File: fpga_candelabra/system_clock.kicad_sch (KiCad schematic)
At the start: 21 parts, among them U22 CDCM6208V1, Y2 NX3225GA 25MHz

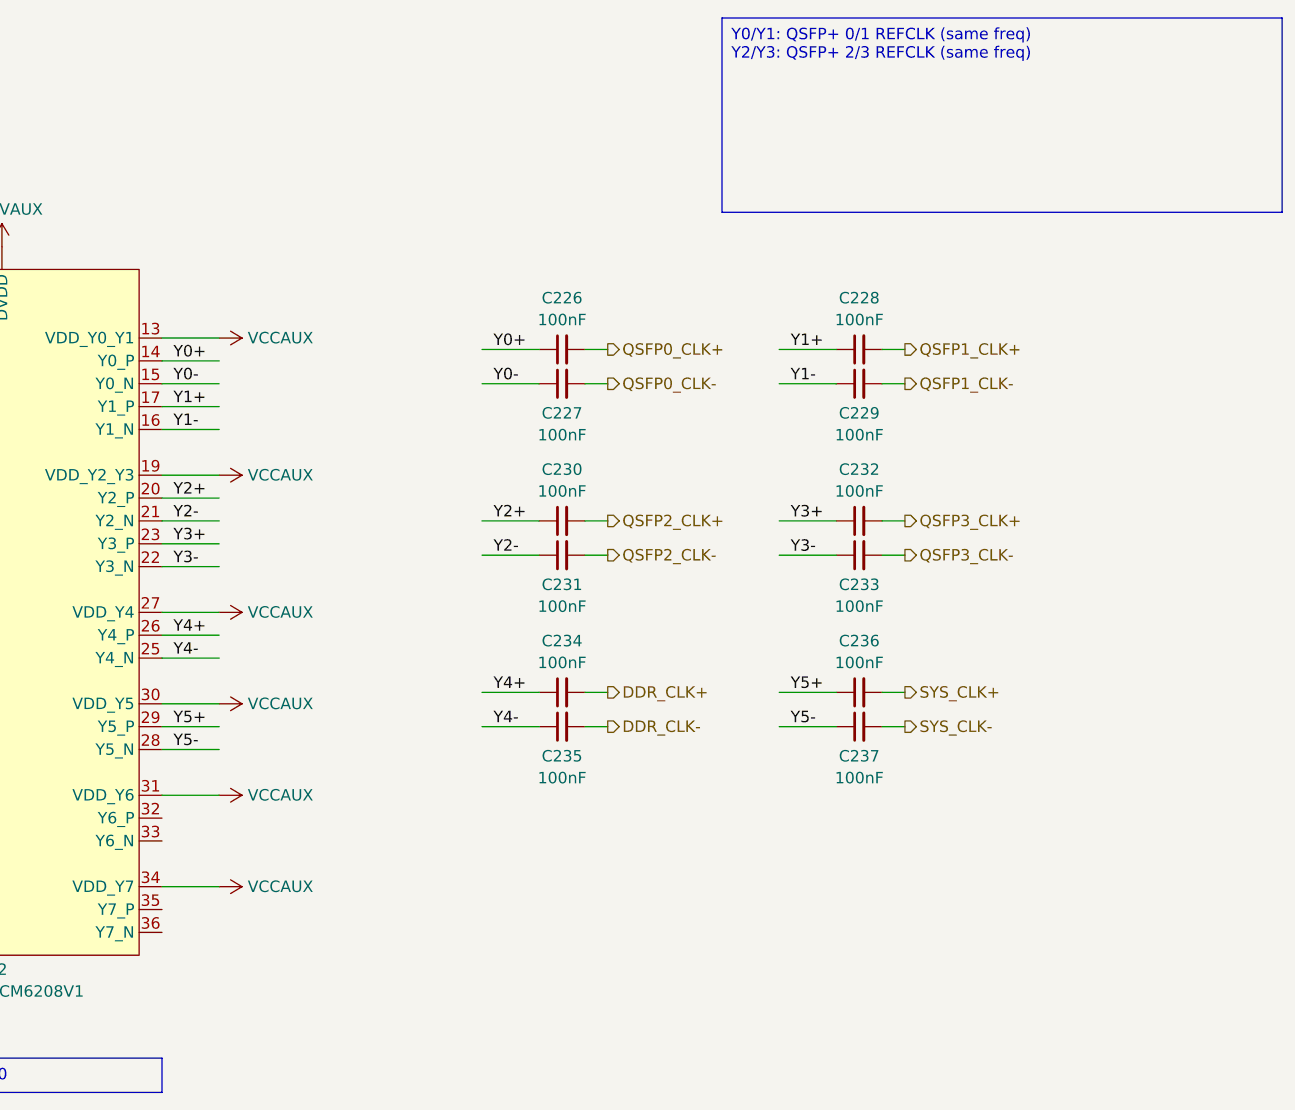
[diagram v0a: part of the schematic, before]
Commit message: candelabra: add i-pex extension ports, remove FMC1
* update bank/mgt allocation
* add basic pcb floorplanning

Signed-off-by: Yichuan Gao <gaoyichuan000@gmail.com>
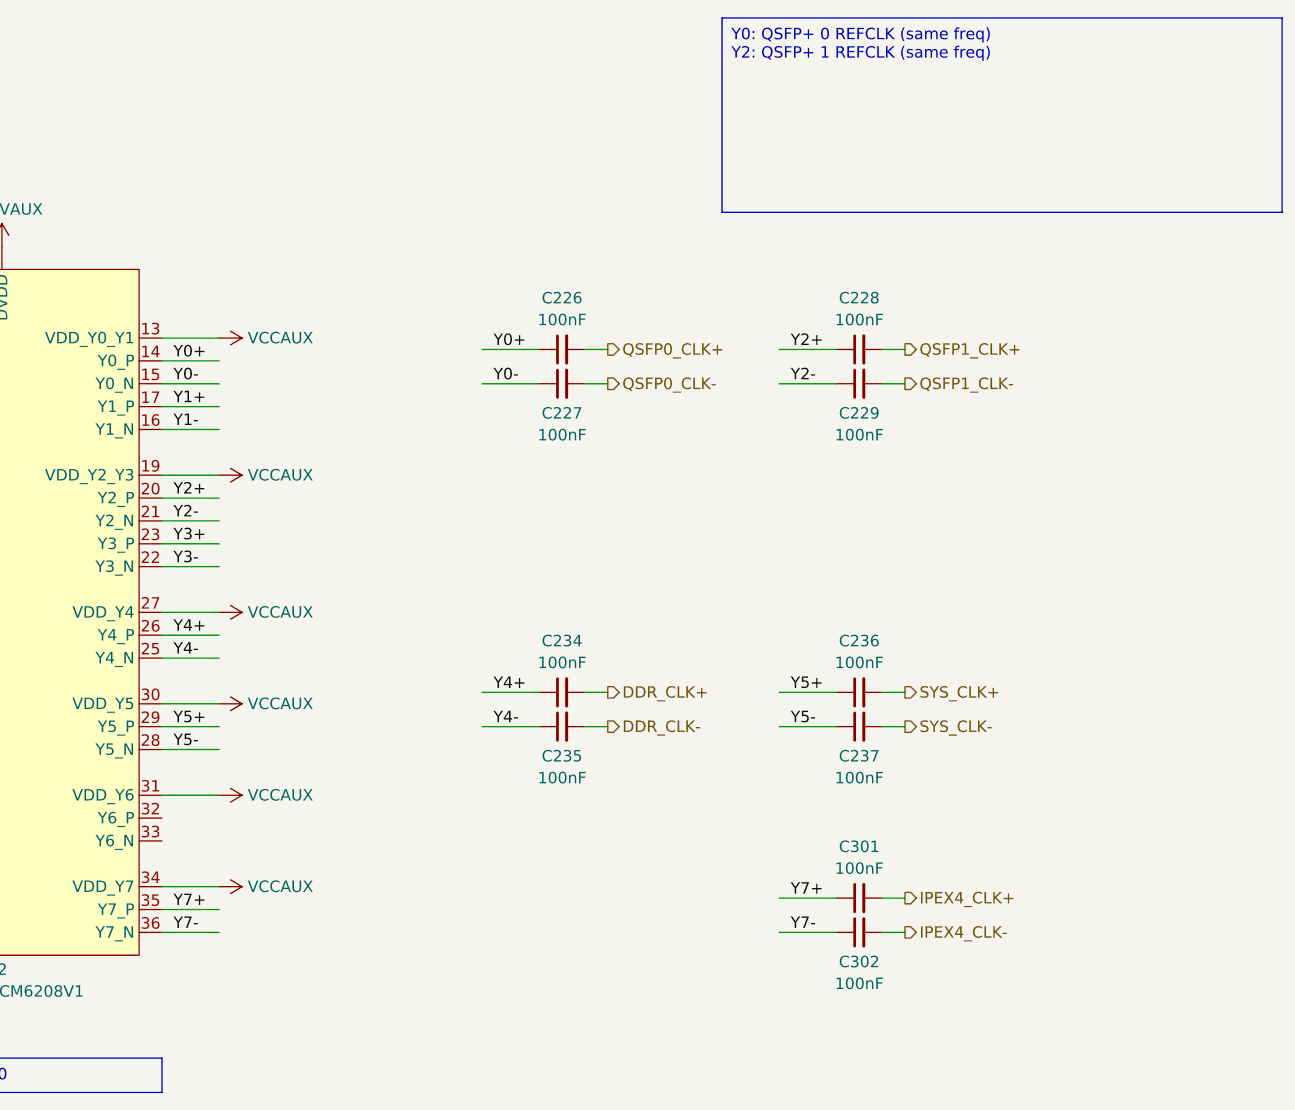
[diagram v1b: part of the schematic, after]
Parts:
- removed C230, C231, C232, C233: 100nF, Capacitor_SMD:C_0402_1005Metric, symbol Device:C_Small
- added C301, C302: 100nF, Capacitor_SMD:C_0402_1005Metric, symbol Device:C_Small
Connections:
- net Y1+: no longer C228.1
- net Y1-: no longer C229.1
- net Y2+: now also C228.1
- net Y2-: now also C229.1
- net Y7+: now reaches U22.35 (Y7_P)
- net Y7+: now also C301.1
- net Y7-: now reaches U22.36 (Y7_N)
- net Y7-: now also C302.1
- new net IPEX4_CLK+: C301.2
- new net IPEX4_CLK-: C302.2

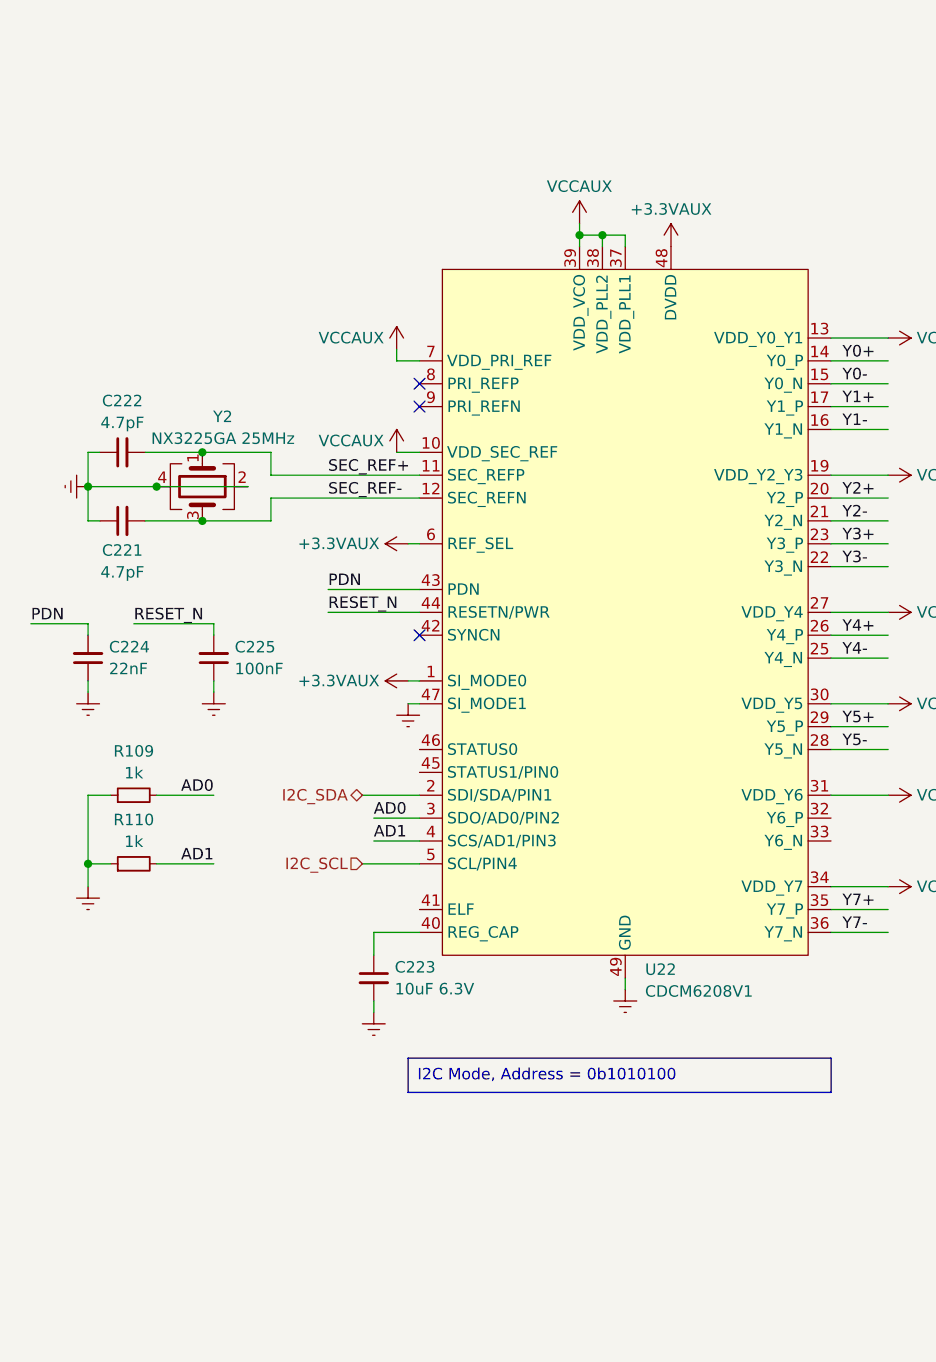
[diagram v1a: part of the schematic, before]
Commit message: fpga_candelabra: major revision
* Finish DDR4 & QSFP+ & PCIe layout
* Change FMC to LPC
* Add mikroBUS extension
* 12V input & PDN updates
* FPGA config updates

Signed-off-by: Yichuan Gao <gaoyichuan000@gmail.com>
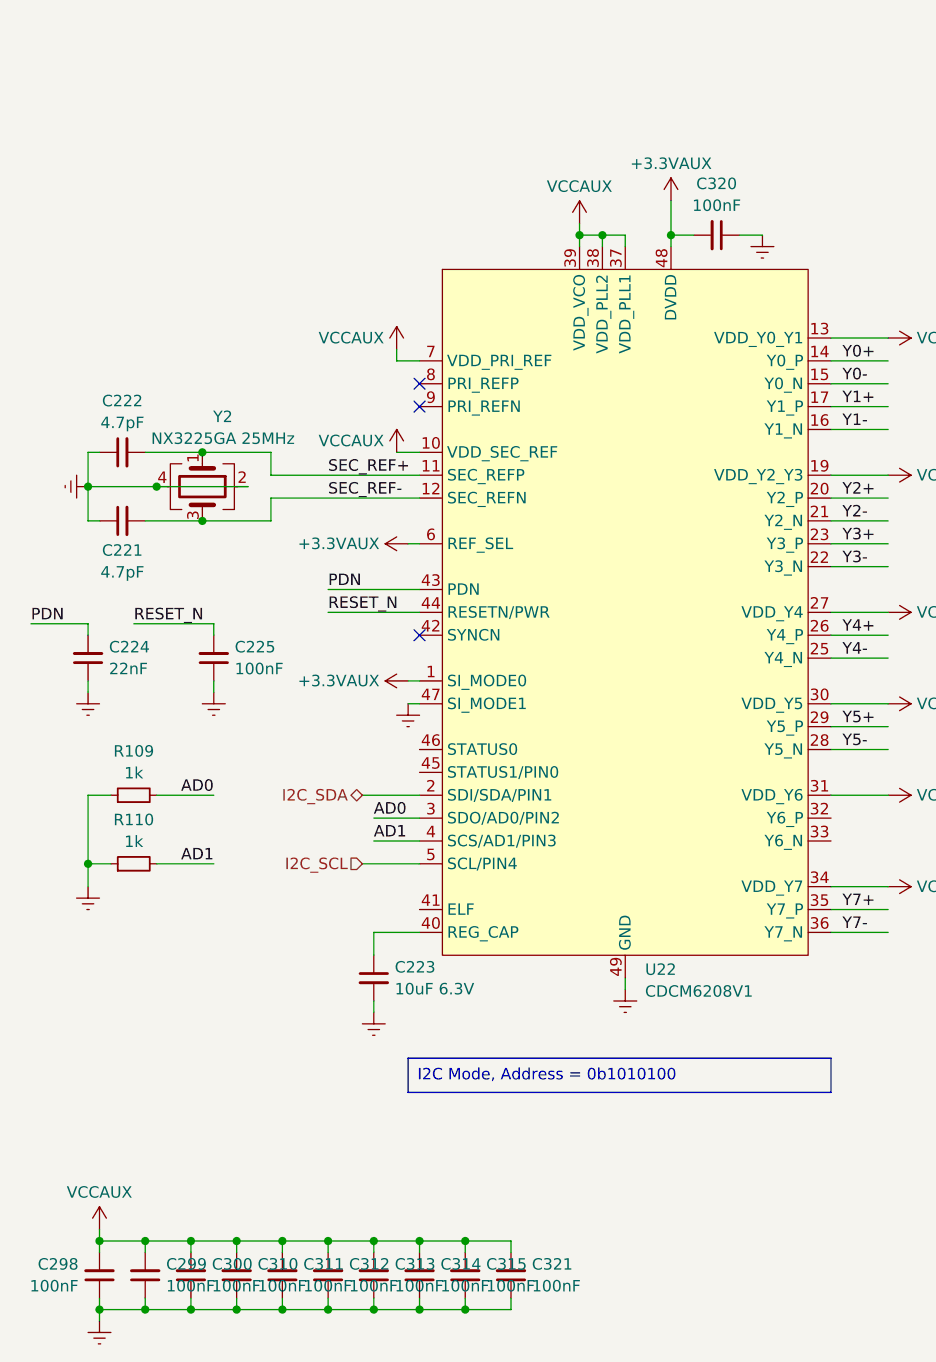
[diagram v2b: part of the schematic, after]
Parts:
- added C298, C299, C300, C310, C311, C312, C313, C314, C315, C320, C321: 100nF, Capacitor_SMD:C_0402_1005Metric, symbol Device:C_Small
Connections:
- net +3.3VAUX: now also C320.2
- net Earth: now also C298.1, C299.1, C300.1, C310.1, C311.1, C312.1, C313.1, C314.1, C315.1, C320.1, C321.1
- net VCCAUX: now also C298.2, C299.2, C300.2, C310.2, C311.2, C312.2, C313.2, C314.2, C315.2, C321.2

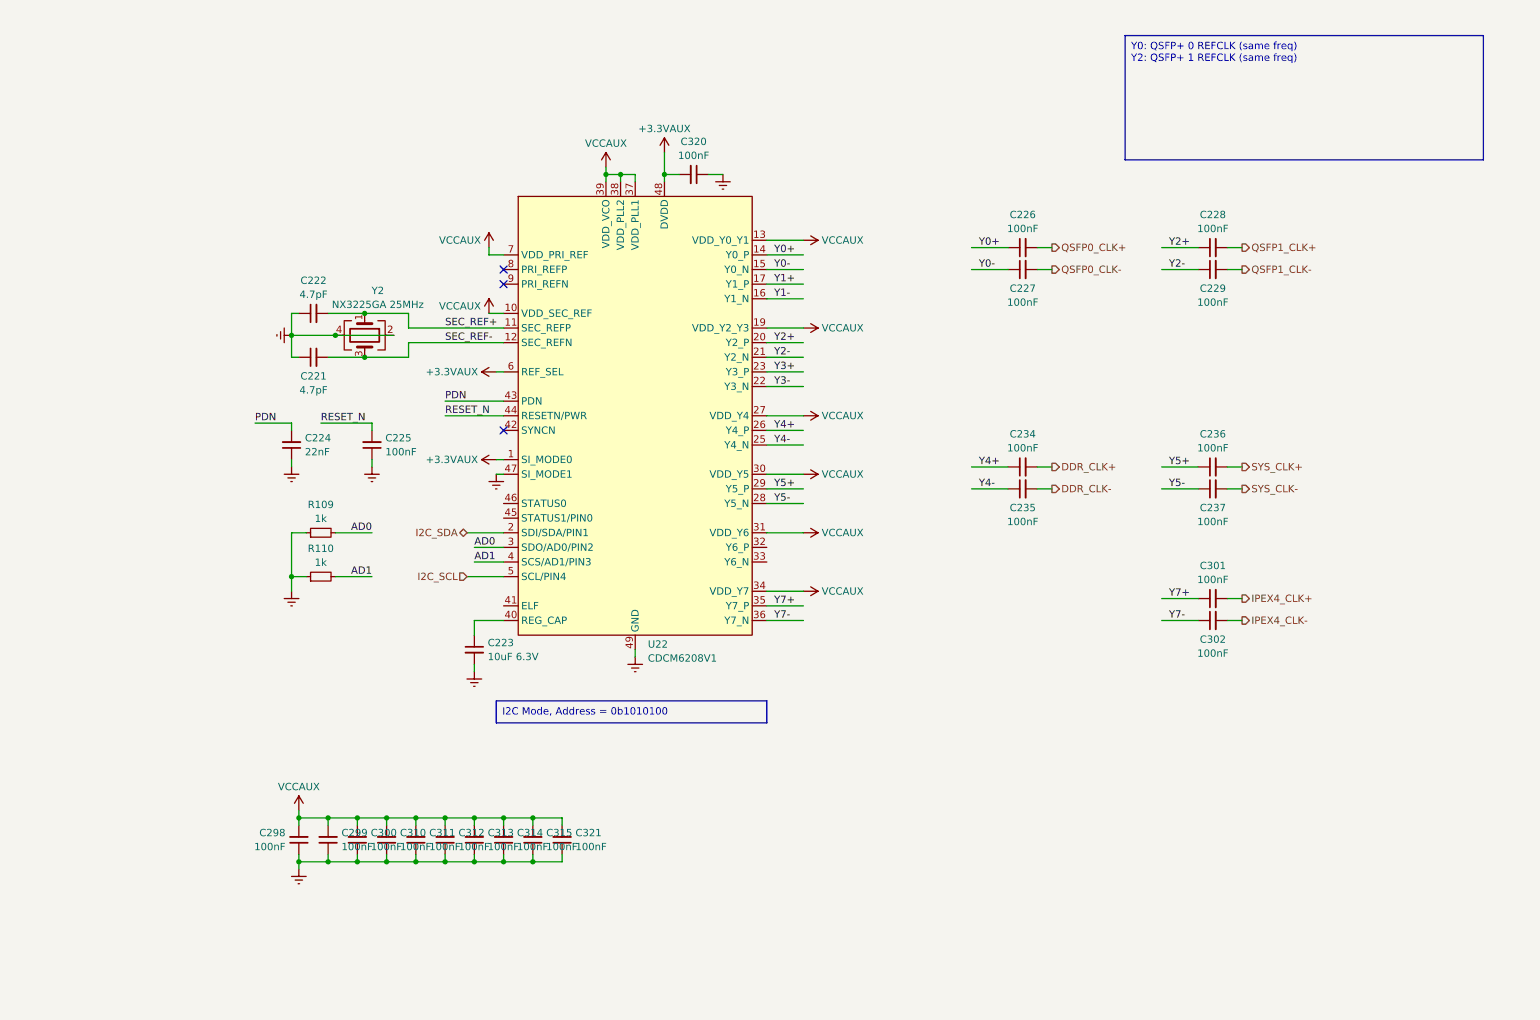
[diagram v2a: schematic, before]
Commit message: fpga_candelabra: sch & layout v0.5, pass basic ERC & DRC
Signed-off-by: Yichuan Gao <gaoyichuan000@gmail.com>
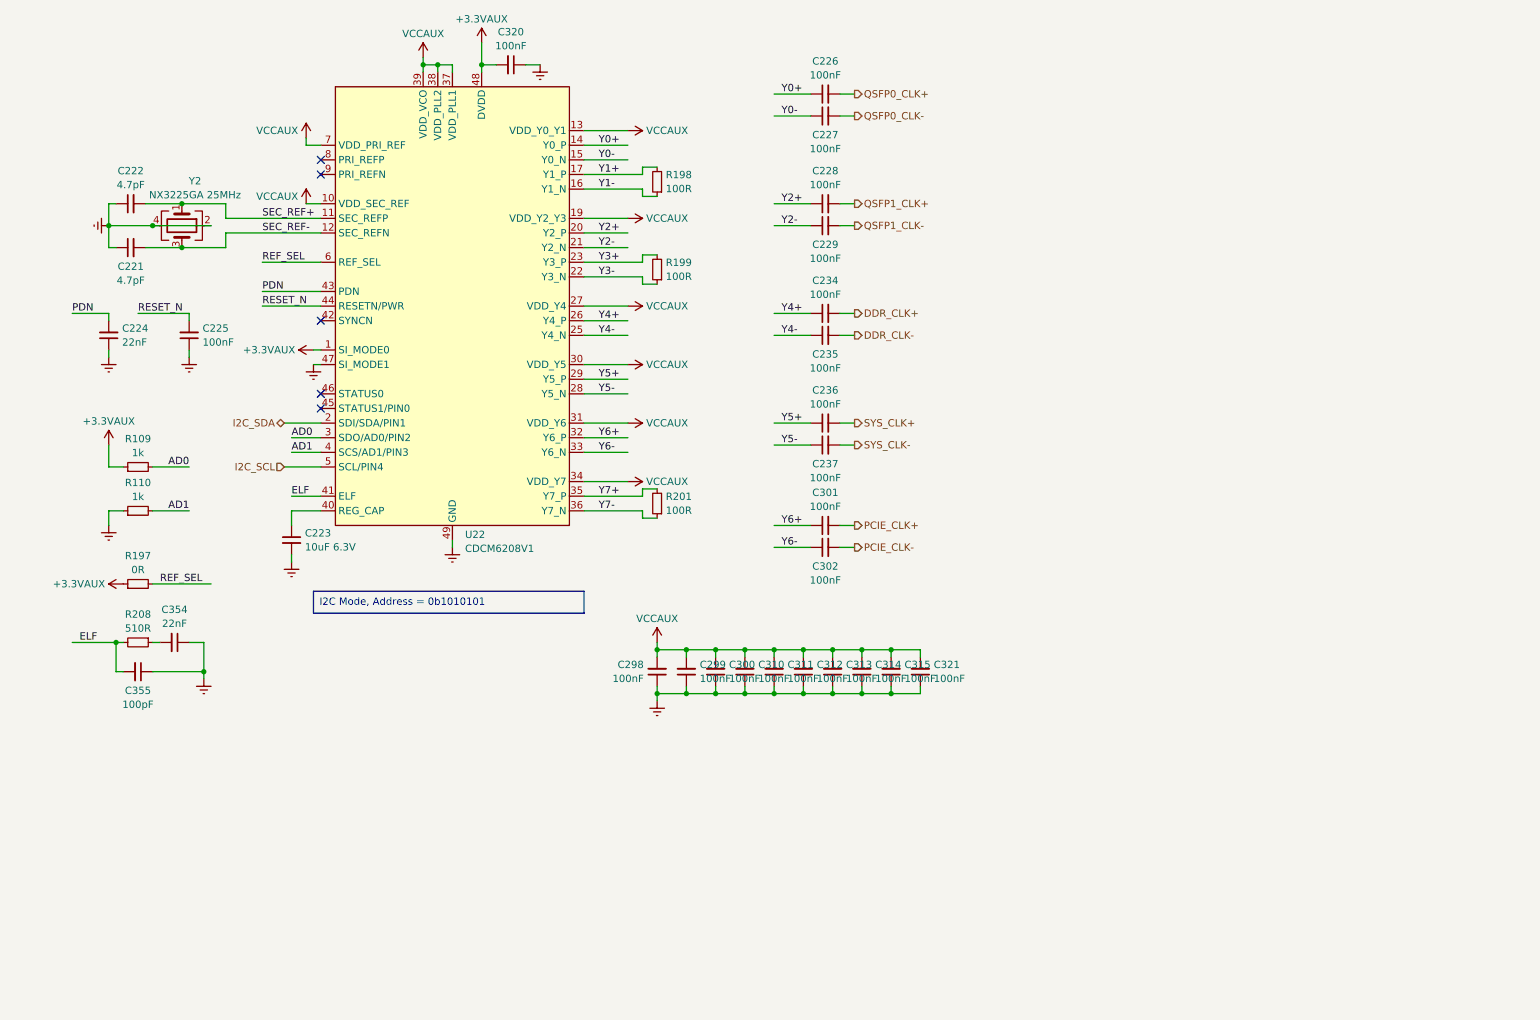
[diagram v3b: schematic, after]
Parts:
- added C354: 22nF, Capacitor_SMD:C_0402_1005Metric, symbol Device:C_Small
- added C355: 100pF, Capacitor_SMD:C_0402_1005Metric, symbol Device:C_Small
- added R197: 0R, Resistor_SMD:R_0402_1005Metric, symbol Device:R_Small
- added R198, R199, R201: 100R, Resistor_SMD:R_0402_1005Metric, symbol Device:R_Small
- added R208: 510R, Resistor_SMD:R_0402_1005Metric, symbol Device:R_Small
- U22: footprint Package_DFN_QFN:Texas_RGZ0048A_VQFN-48-1EP_7x7mm_P0.5mm_EP5.15x5.15mm -> Package_DFN_QFN:Texas_RGZ0048A_VQFN-48-1EP_7x7mm_P0.5mm_EP5.15x5.15mm_ThermalVias
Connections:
- net +3.3VAUX: now also R109.1, R197.1; no longer U22.6 (REF_SEL)
- net Earth: now also C354.1, C355.1; no longer R109.1
- net Y1+: now also R198.2
- net Y1-: now also R198.1
- net Y3+: now also R199.2
- net Y3-: now also R199.1
- net Y7+: now also R201.2; no longer C301.1
- net Y7-: now also R201.1; no longer C302.1
- net Y6+: now reaches U22.32 (Y6_P)
- net Y6+: now also C301.1
- net Y6-: now reaches U22.33 (Y6_N)
- net Y6-: now also C302.1
- net ELF: now reaches U22.41 (ELF)
- net ELF: now also C355.2, R208.2
- net IPEX4_CLK+ renamed PCIE_CLK+
- net IPEX4_CLK- renamed PCIE_CLK-
- new net: C354.2, R208.1
- new net REF_SEL: R197.2, U22.6 (REF_SEL)
- no-connect marks 3 -> 5
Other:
- moved on the sheet: C221, C222, C223, C224, C225, C226, C227, C228, C229, C234, C235, C236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
